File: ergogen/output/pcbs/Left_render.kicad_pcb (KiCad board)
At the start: 2 copper layers, 130.3 x 105.3 mm, 44 parts

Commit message: update config
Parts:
- MCU1: footprint 1:xiao_smd_xl_cutout -> 1:xiao_smd_xl_cutout_minimal
- SW1: footprint 1:PCM12SMTR_front -> 1:1208YD
- moved SW1 58.6 mm to (175.2, 34.2), turned to 0 degrees
- moved S19 58.0 mm to (118.2, 31.4)
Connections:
- CONN1 pad 1: BAT_P -> BAT_CONN
- MCU1 pad 10: D9 -> C3
- MCU1 pad 11: C0 -> C4
- MCU1 pad 17: GND -> RST
- MCU1 pad 3: D2 -> R3
- MCU1 pad 4: D3 -> R2
- MCU1 pad 5: D4 -> R1
- MCU1 pad 6: D5 -> R0
- MCU1 pad 7: D6 -> C0
- MCU1 pad 8: D7 -> C1
- MCU1 pad 9: D8 -> C2
- SW1 pad 1: (no net) -> BAT
- SW1 pad 2: RAW -> BAT_CONN
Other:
- outline, holes or cut-outs redrawn
- board text removed: "ON"

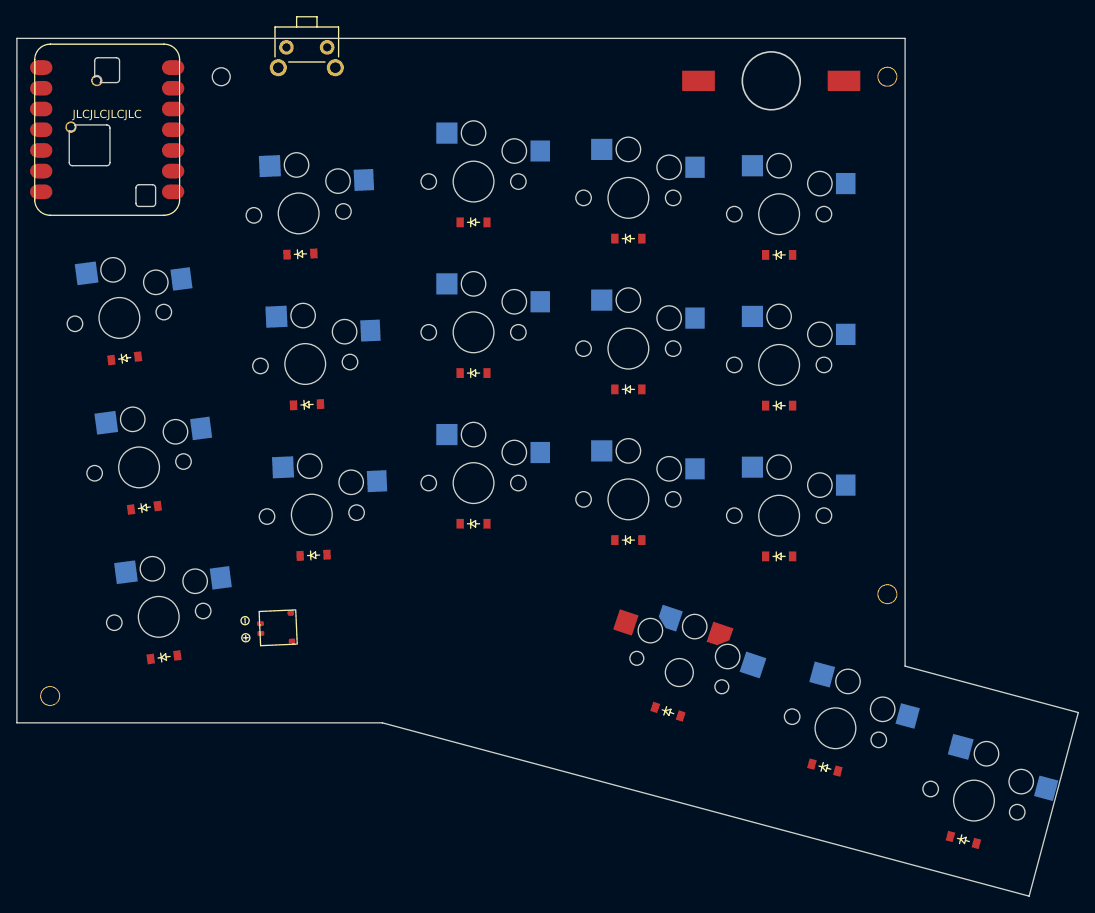
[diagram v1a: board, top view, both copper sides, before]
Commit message: add battery outlines to pcb
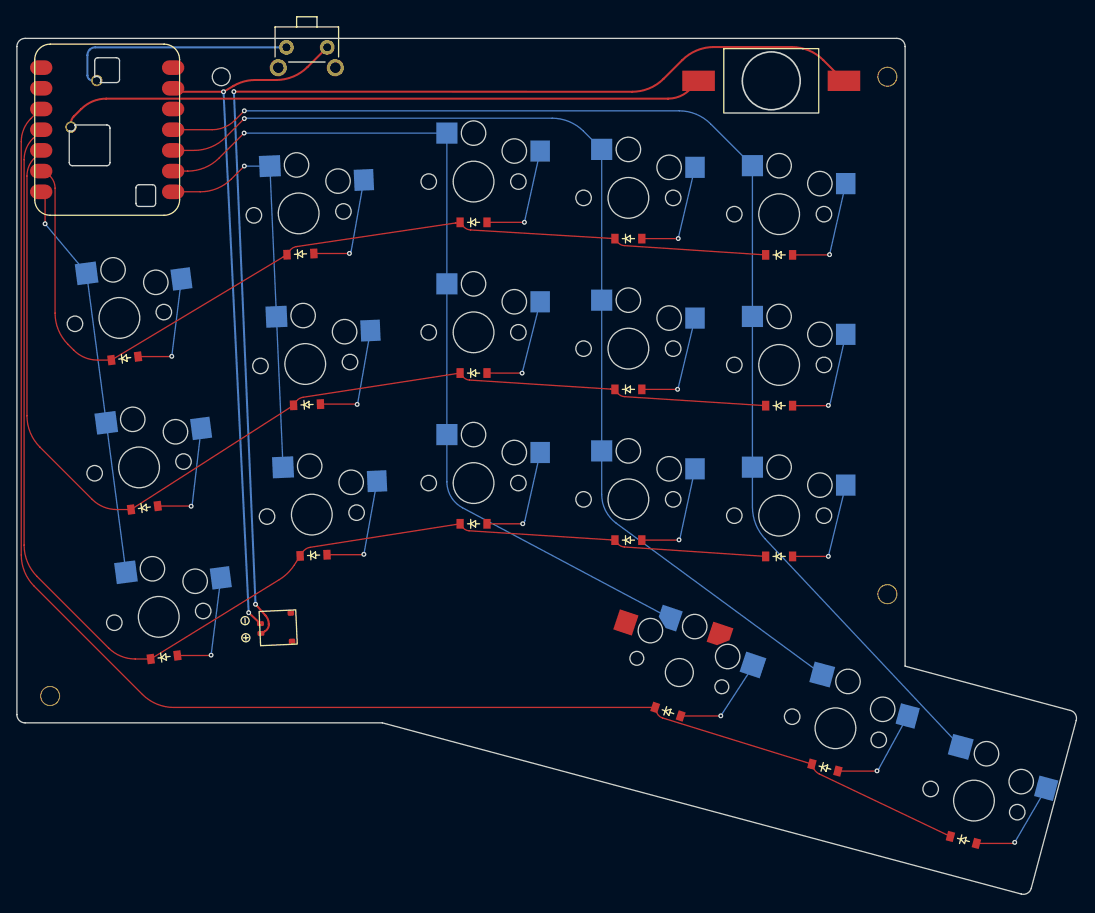
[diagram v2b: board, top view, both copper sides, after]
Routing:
- net R3: track 0.00 -> 182.6 mm
- net C4: track 0.00 -> 156.1 mm, vias 0 -> 1
- net R2: track 0.00 -> 155.1 mm
- net BAT_CONN: track 0.00 -> 145.6 mm, vias 0 -> 2
- net R1: track 0.00 -> 134.9 mm
- net C3: track 0.00 -> 133.5 mm, vias 0 -> 1
- net R0: track 0.00 -> 113.1 mm
- net C2: track 0.00 -> 111.4 mm, vias 0 -> 1
- net GND: track 0.00 -> 87.2 mm, vias 0 -> 2
- net BAT: track 0.00 -> 79.5 mm
- net C1: track 0.00 -> 50.4 mm, vias 0 -> 1
- net C0: track 0.00 -> 48.9 mm, vias 0 -> 1
- net RST: track 0.00 -> 28.9 mm
- net pinky_home: track 0.00 -> 13.8 mm, vias 0 -> 1
- net ring_home: track 0.00 -> 13.7 mm, vias 0 -> 1
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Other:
- board size 130.3 x 105.3 mm -> 130 x 105 mm
- board text added: "2024.10.12"
- board text added: "dohn-joh"
- board text added: "liaison"
- board text removed: "JLCJLCJLCJLC"
